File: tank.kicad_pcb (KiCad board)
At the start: 4 copper layers, 70 x 70 mm, 163 parts, among them IC1 STUSB4531QTR, IC2 DCP3601NMR, IC3 DCP3601NMR, IC4 BQ24800RUYR, J1 629722000214, J10 Conn_DET_RIGHT, J2 B2B-XH-A_LF__SN_, J3 B2B-XH-A_LF__SN_, J4 Conn_ENC_LEFT, J5 Conn_ENC_RIGHT, J6 S4B-XH-A-1, J7 HC-05, J8 PROG, J9 Conn_DET_LEFT, SW1 B3S-1000, SW2 B3S-1000, SW3 B3S-1000, SW4 B3S-1000, U1 XSM6K519NW, U10 LMD18200, U11 LMD18200, U12 SQJ459EP-T2_BE3, U13 SQJ459EP-T2_BE3, U2 XSM6K519NW, U3 XSM6K519NW, U4 XSM6K519NW, U5 XSM6K519NW, U6 BQ76905RGRR, U7 XSM6K519NW, U8 XSM6K519NW, U9 STM32G431KBT6

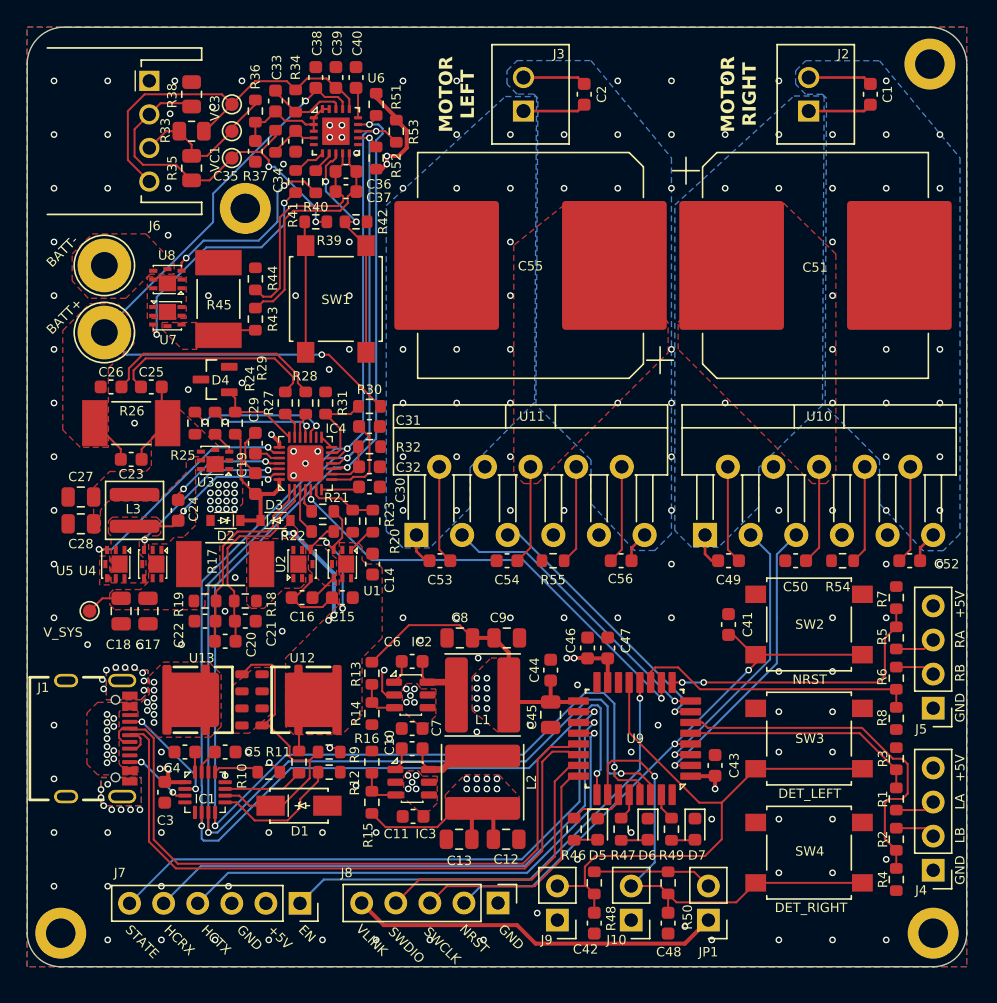
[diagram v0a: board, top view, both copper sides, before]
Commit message: Léger remapping du stm32.
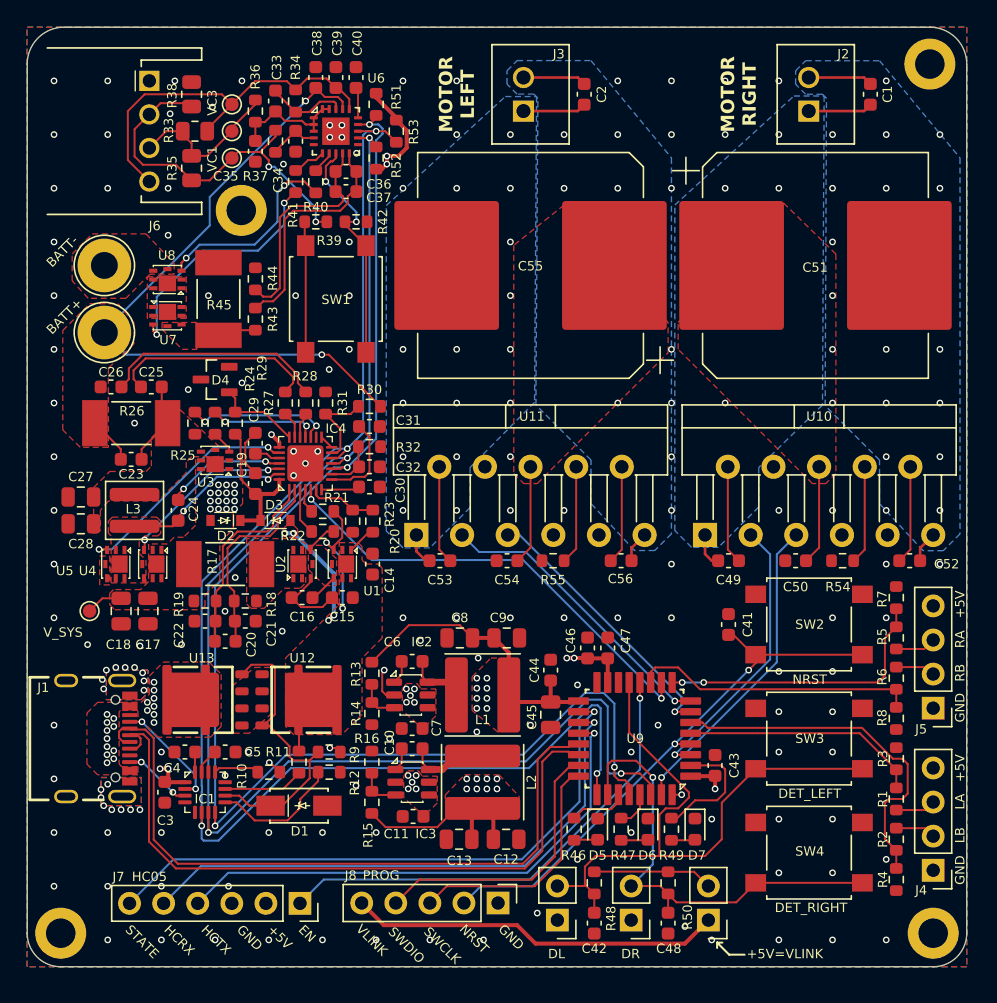
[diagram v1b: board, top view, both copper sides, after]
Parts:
- moved REF** 0.34 mm to (130.9, 79.7)
- moved R33 0.25 mm to (127.5, 73.8)
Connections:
- R47 pad 2: Net-(U9-PB5) -> Net-(U9-PB6)
- R49 pad 2: Net-(U9-PB8-BOOT0) -> Net-(U9-PF0-OSC_IN)
- U9 pad 2: /motor_right/PWM -> Net-(U9-PF0-OSC_IN)
- U9 pad 28: Net-(U9-PB5) -> /power/~{ALERT}
- U9 pad 29: /power/~{ALERT} -> Net-(U9-PB6)
- U9 pad 31: Net-(U9-PB8-BOOT0) -> /motor_right/PWM
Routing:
- net Net-(U9-PF0-OSC_IN): track 0.00 -> 9.19 mm
- net /stm32/DETECT_LEFT: track 44.0 -> 47.4 mm
- net Net-(U9-PB6): track 0.00 -> 2.75 mm
- net Net-(U9-PB8-BOOT0): track 2.06 -> 0.00 mm
- net Net-(U9-PB5): track 1.99 -> 0.00 mm
- net /motor_right/PWM: track 22.2 -> 23.5 mm
- net /power/~{ALERT}: track 105.2 -> 104.4 mm
- net GND: track 8.22 -> 8.93 mm, vias 190 -> 191
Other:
- board text added: "+5V=VLINK"
- board text added: "DL"
- board text added: "DR"
- board text added: "HC05"
- board text added: "PROG"

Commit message: Modifications mineurs du schéma. Passage sous Kicad 10 ok. Finalisations PCB (teardrops, arrondis)
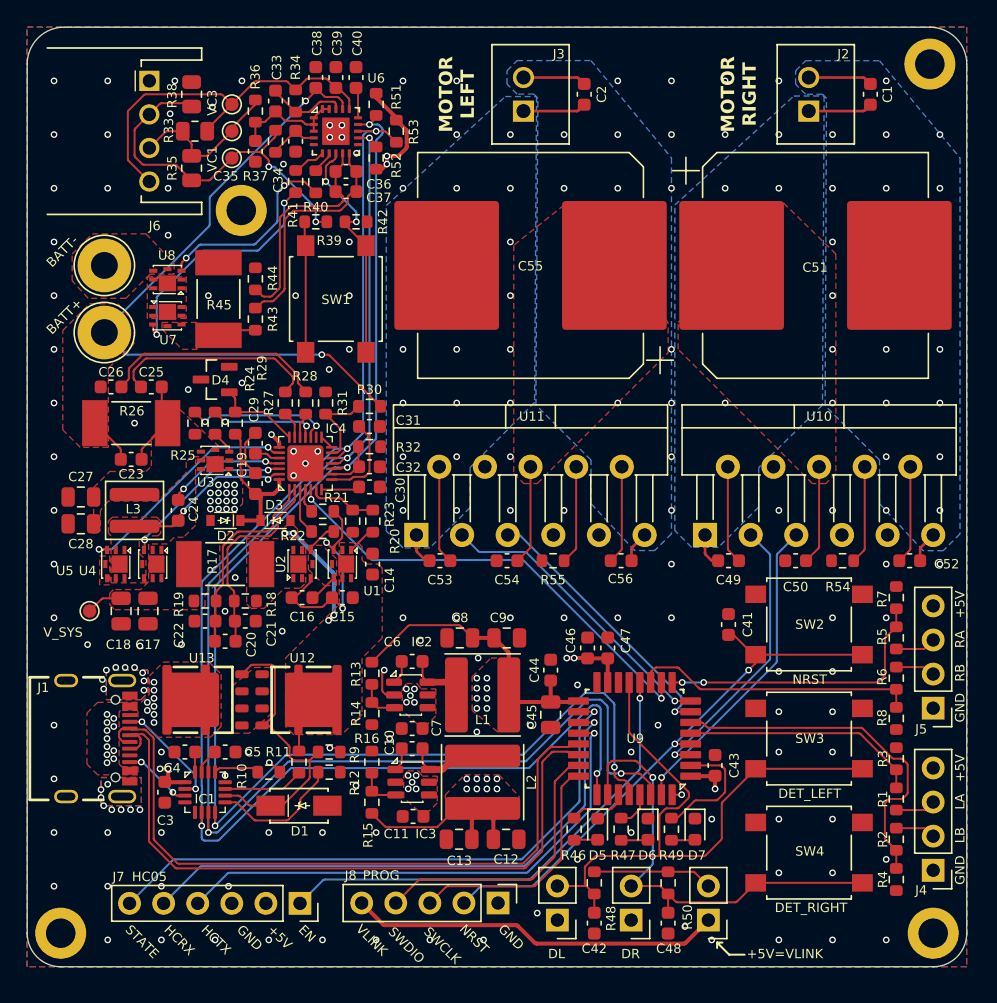
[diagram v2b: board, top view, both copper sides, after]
